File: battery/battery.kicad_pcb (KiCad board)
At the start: 2 copper layers, 88.9 x 63.5 mm, 53 parts, among them J1 batt_1, J2 batt_2, J3 batt_3, J4 batt_4, J5 reed_switch, J6 toPcb+, J7 toPcb-, J8 on_signal, Q1 batt1_sw, Q2 batt2_sw, Q3 batt3_sw, Q4 batt4_sw, Q5 BC817-25, U1 LM1117-5.0, U2 LTV-817S

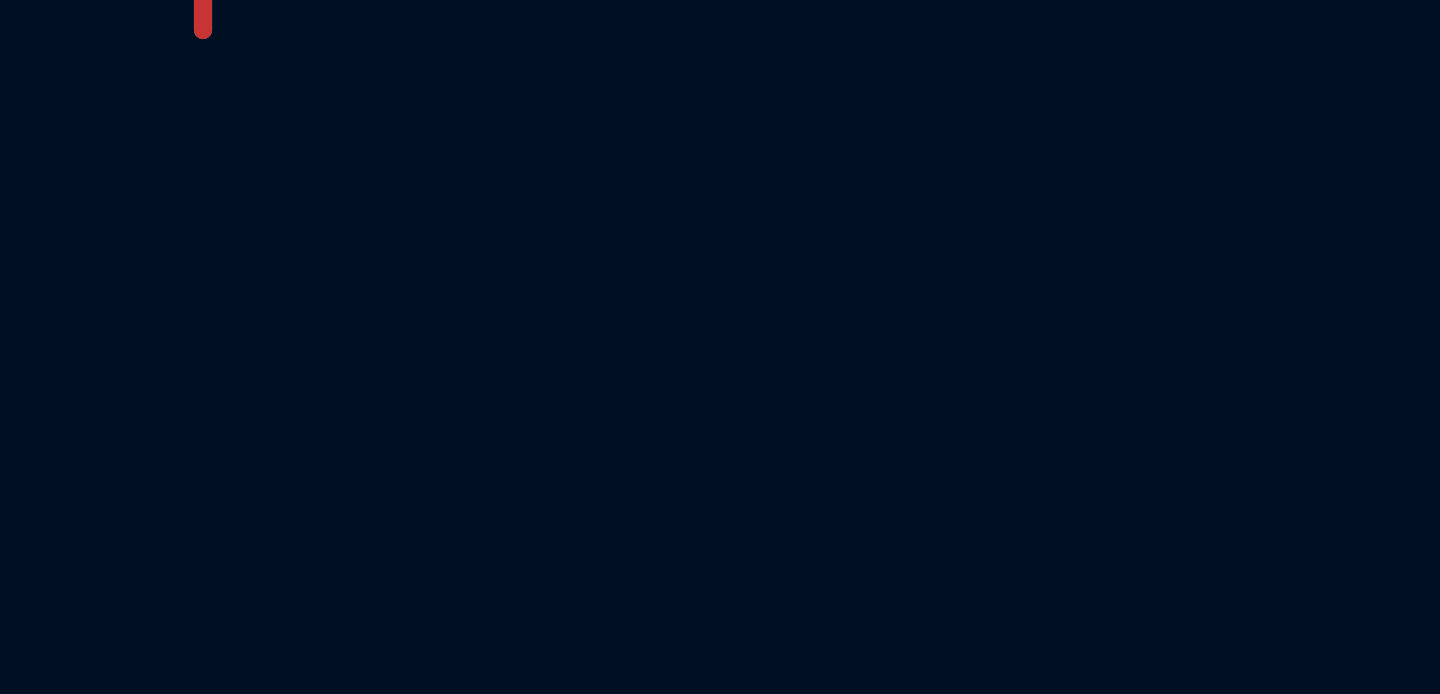
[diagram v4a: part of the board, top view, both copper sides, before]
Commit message: bus bar  outline
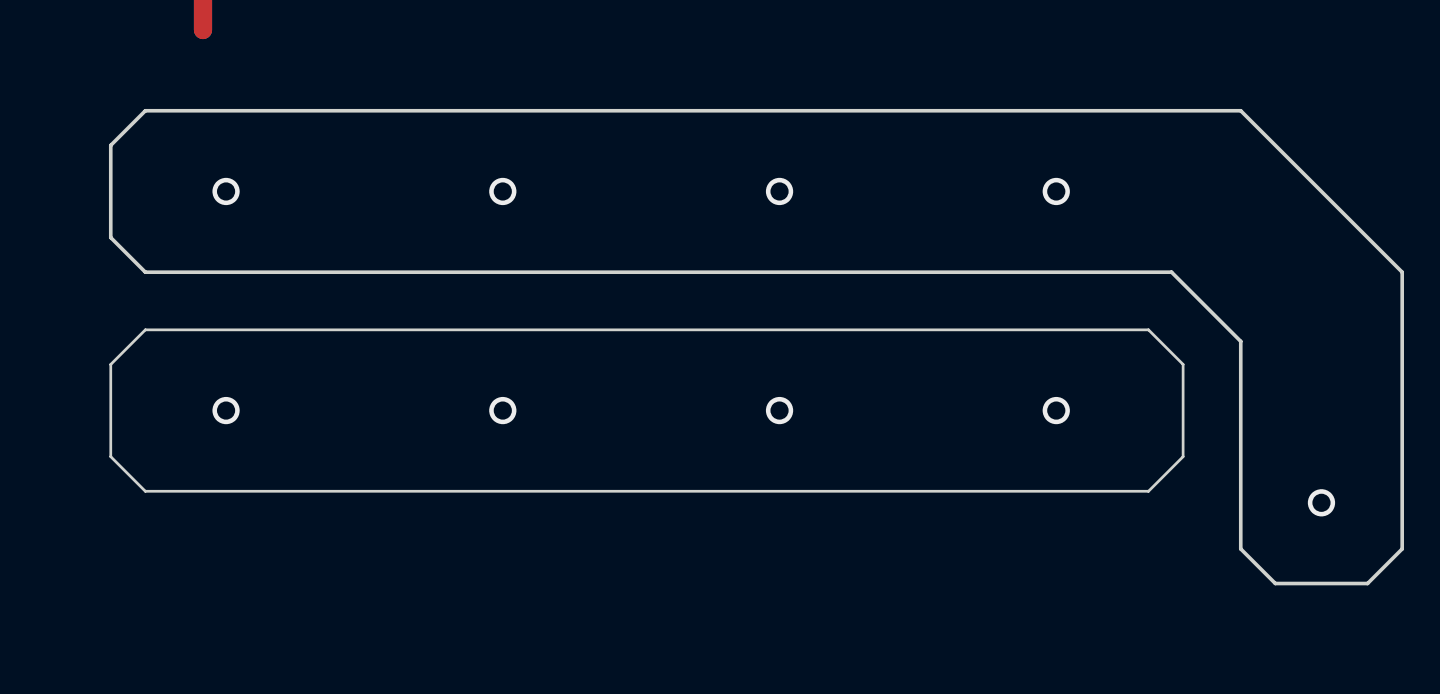
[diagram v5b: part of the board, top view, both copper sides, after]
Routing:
- net (no net): vias 0 -> 9
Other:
- board size 88.9 x 63.5 mm -> 170.2 x 63.5 mm
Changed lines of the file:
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@@
   (general
     (thickness 1.6)
-    (drawings 13)
-    (tracks 233)
+    (drawings 33)
+    (tracks 242)
     (zones 0)
     (modules 53)
@@
     )
   )
+  (gr_line (start 198.12 76.835) (end 200.025 74.93) (layer Edge.Cuts) (width 0.15))
+  (gr_line (start 198.12 81.915) (end 198.12 76.835) (layer Edge.Cuts) (width 0.15))
+  (gr_line (start 200.025 83.82) (end 198.12 81.915) (layer Edge.Cuts) (width 0.15))
+  (gr_line (start 255.27 83.82) (end 200.025 83.82) (layer Edge.Cuts) (width 0.15))
+  (gr_line (start 257.175 81.915) (end 255.27 83.82) (layer Edge.Cuts) (width 0.15))
+  (gr_line (start 257.175 76.835) (end 257.175 81.915) (layer Edge.Cuts) (width 0.15))
+  (gr_line (start 255.27 74.93) (end 257.175 76.835) (layer Edge.Cuts) (width 0.15))
+  (gr_line (start 200.025 74.93) (end 255.27 74.93) (layer Edge.Cuts) (width 0.15))
+  (gr_line (start 260.35 86.995) (end 260.35 75.565) (layer Edge.Cuts) (width 0.2))
+  (gr_line (start 198.12 69.85) (end 198.12 64.77) (layer Edge.Cuts) (width 0.2))
+  (gr_line (start 256.54 71.755) (end 200.025 71.755) (layer Edge.Cuts) (width 0.2))
+  (gr_line (start 260.35 75.565) (end 256.54 71.755) (layer Edge.Cuts) (width 0.2))
+  (gr_line (start 262.255 88.9) (end 260.35 86.995) (layer Edge.Cuts) (width 0.2))
+  (gr_line (start 198.12 64.77) (end 200.025 62.865) (layer Edge.Cuts) (width 0.2))
+  (gr_line (start 200.025 62.865) (end 260.35 62.865) (layer Edge.Cuts) (width 0.2))
+  (gr_line (start 200.025 71.755) (end 198.12 69.85) (layer Edge.Cuts) (width 0.2))
+  (gr_line (start 260.35 62.865) (end 269.24 71.755) (layer Edge.Cuts) (width 0.2))
+  (gr_line (start 269.24 86.995) (end 267.335 88.9) (layer Edge.Cuts) (width 0.2))
+  (gr_line (start 267.335 88.9) (end 262.255 88.9) (layer Edge.Cuts) (width 0.2))
+  (gr_line (start 269.24 71.755) (end 269.24 86.995) (layer Edge.Cuts) (width 0.2))
   (gr_line (start 99.06 123.825) (end 187.96 123.825) (layer Edge.Cuts) (width 0.2))
   (gr_line (start 99.06 60.325) (end 99.06 123.825) (layer Edge.Cuts) (width 0.2))
@@
   (segment (start 81.28 40.64) (end 81.28 48.26) (width 1) (layer F.Cu) (net 0))
   (segment (start 81.28 48.26) (end 68.58 48.26) (width 1) (layer F.Cu) (net 0))
+  (via (at 234.95 67.31) (size 1.5) (drill 1) (layers F.Cu B.Cu) (net 0))
+  (via (at 264.795 84.455) (size 1.5) (drill 1) (layers F.Cu B.Cu) (net 0))
+  (via (at 250.19 67.31) (size 1.5) (drill 1) (layers F.Cu B.Cu) (net 0))
+  (via (at 204.47 67.31) (size 1.5) (drill 1) (layers F.Cu B.Cu) (net 0))
+  (via (at 219.71 67.31) (size 1.5) (drill 1) (layers F.Cu B.Cu) (net 0))
+  (via (at 234.95 79.375) (size 1.5) (drill 1) (layers F.Cu B.Cu) (net 0))
+  (via (at 250.19 79.375) (size 1.5) (drill 1) (layers F.Cu B.Cu) (net 0))
+  (via (at 219.71 79.375) (size 1.5) (drill 1) (layers F.Cu B.Cu) (net 0))
+  (via (at 204.47 79.375) (size 1.5) (drill 1) (layers F.Cu B.Cu) (net 0))
   (via (at 179.705 83.185) (size 1.5) (drill 1) (layers F.Cu B.Cu) (net 3))
   (via (at 165.1 66.04) (size 1.5) (drill 1) (layers F.Cu B.Cu) (net 3))
